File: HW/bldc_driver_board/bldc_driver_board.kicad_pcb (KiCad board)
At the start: 2 copper layers, 80 x 119.4 mm, 55 parts, among them IC1 DRV8305NPHPR, J1 PWR, J2 N_CN7, J3 N_CN10, J5 Motor, J6 RJ45, J7 RJ45, Q1 STD140N6F7, Q2 STD140N6F7, Q3 STD140N6F7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

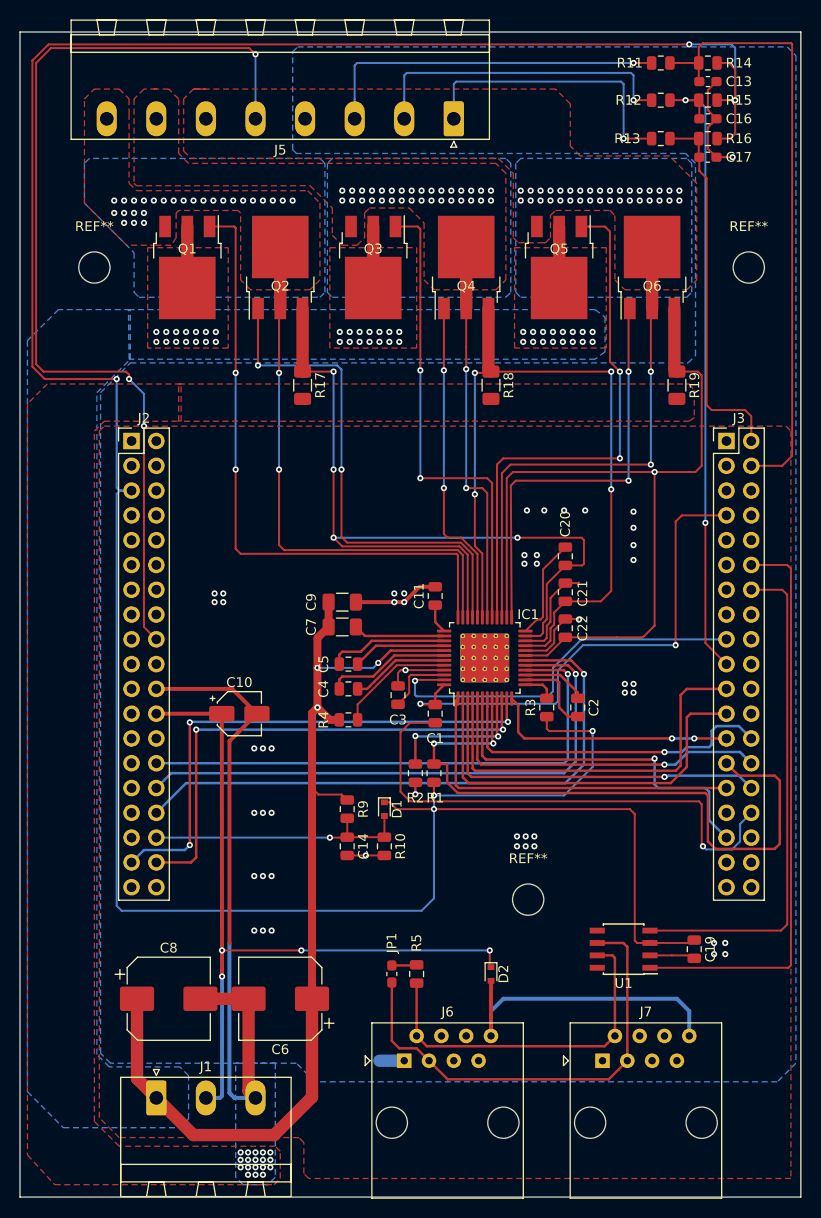
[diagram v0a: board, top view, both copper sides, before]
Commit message: -- Added panels for drill holes
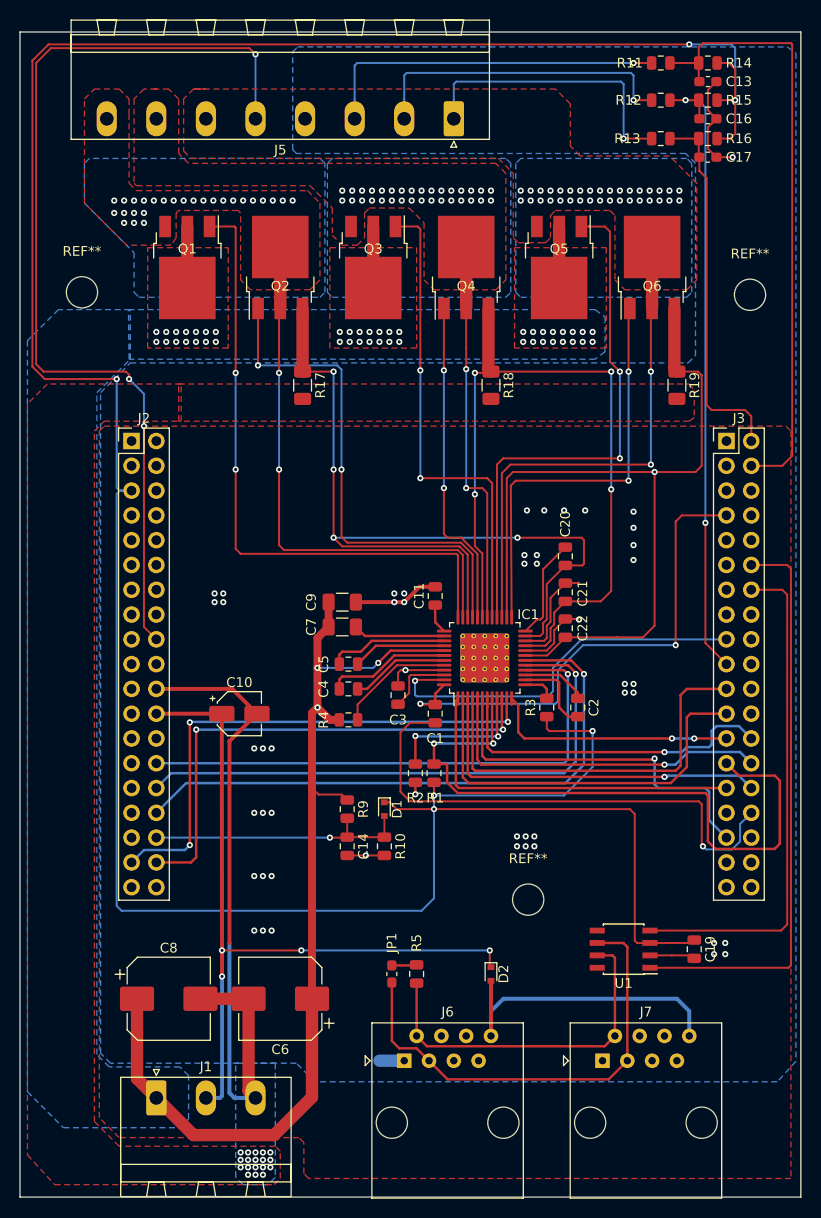
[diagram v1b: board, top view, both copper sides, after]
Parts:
- moved REF** 2.84 mm to (38.1, 73.7)
- moved REF** 2.80 mm to (106.6, 73.9)
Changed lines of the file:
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@@
   )
   (module MountingHole:MountingHole_3.2mm_M3 (layer F.Cu)
-    (at 39.37 71.12)
+    (at 38.1 73.66)
     (descr "Mounting Hole 3.2mm, no annular, M3")
     (tags "mounting hole 3.2mm no annular m3")
@@
   )
   (module MountingHole:MountingHole_3.2mm_M3 (layer F.Cu)
-    (at 106.426 71.12)
+    (at 106.553 73.914)
     (descr "Mounting Hole 3.2mm, no annular, M3")
     (tags "mounting hole 3.2mm no annular m3")
@@
         (xy 43.053 80.899) (xy 100.203 80.899) (xy 100.965 80.137) (xy 100.965 60.452) (xy 99.949 59.436)
         (xy 60.071 59.436) (xy 59.69 59.055) (xy 59.69 49.022) (xy 60.198 48.514) (xy 110.363 48.514)
-        (xy 111.252 49.403) (xy 111.252 152.654) (xy 109.347 154.559)
+        (xy 111.252 49.149) (xy 111.252 152.4635) (xy 109.347 154.559)
       )
     )
@@
       )
     )
+  )
+  (zone (net 0) (net_name "") (layers F&B.Cu) (hatch full 0.508)
+    (connect_pads (clearance 0.813))
+    (min_thickness 0.254)
+    (keepout (tracks not_allowed) (vias not_allowed) (copperpour not_allowed))
+    (fill (arc_segments 16) (thermal_gap 0.508) (thermal_bridge_width 0.508))
+    (polygon
+      (pts
+        (xy 80.01 139.192) (xy 80.01 132.588) (xy 80.264 132.334) (xy 80.518 132.08) (xy 87.249 132.08)
+        (xy 87.503 132.334) (xy 87.63 132.461) (xy 87.63 139.319) (xy 87.503 139.446) (xy 87.249 139.7)
+        (xy 80.518 139.7) (xy 80.264 139.446)
+      )
+    )
+  )
+  (zone (net 0) (net_name "") (layers F&B.Cu) (hatch edge 0.508)
+    (connect_pads (clearance 0.813))
+    (min_thickness 0.254)
+    (keepout (tracks not_allowed) (vias not_allowed) (copperpour not_allowed))
+    (fill (arc_segments 16) (thermal_gap 0.508) (thermal_bridge_width 0.508))
+    (polygon
+      (pts
+        (xy 109.728 70.104) (xy 102.743 70.104) (xy 102.743 70.739) (xy 102.743 77.597) (xy 109.728 77.597)
+        (xy 110.109 77.216) (xy 110.236 77.089) (xy 110.236 70.612) (xy 109.982 70.358)
+      )
+    )
+  )
+  (zone (net 0) (net_name "") (layers F&B.Cu) (hatch edge 0.508)
+    (connect_pads (clearance 0.813))
+    (min_thickness 0.254)
+    (keepout (tracks not_allowed) (vias not_allowed) (copperpour not_allowed))
+    (fill (arc_segments 16) (thermal_gap 0.508) (thermal_bridge_width 0.508))
+    (polygon
+      (pts
+        (xy 34.29 76.962) (xy 34.29 69.85) (xy 42.418 69.85) (xy 42.418 75.438) (xy 41.91 75.946)
+        (xy 41.91 76.962) (xy 41.402 77.47) (xy 34.798 77.47)
+      )
+    )

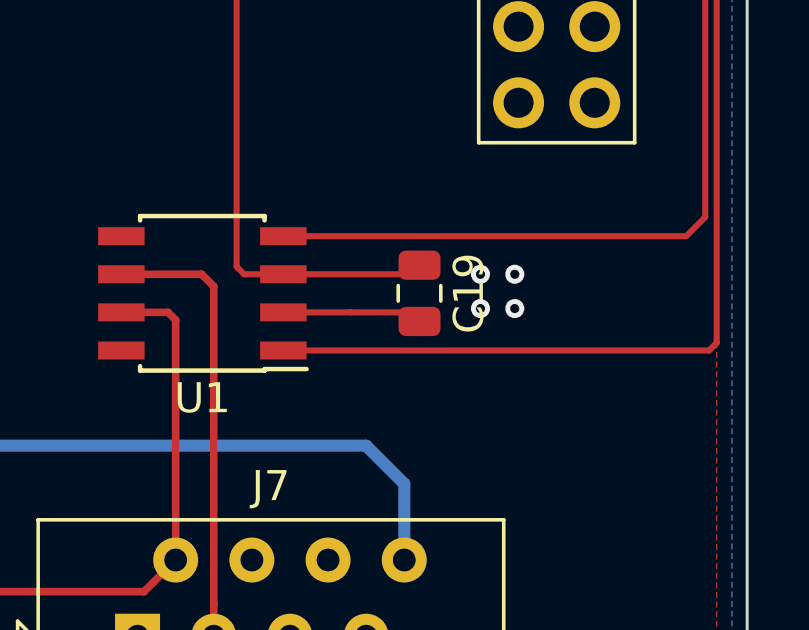
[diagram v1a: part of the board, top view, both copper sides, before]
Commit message: -- Fixed unwired CAN chip
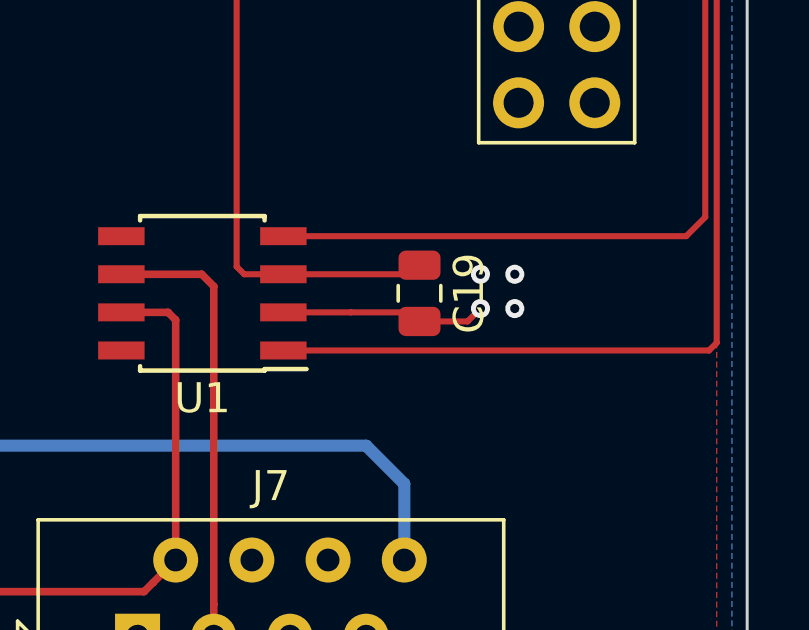
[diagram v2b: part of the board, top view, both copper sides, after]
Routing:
- net GND: track 144.6 -> 146.8 mm
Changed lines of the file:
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@@
     (thickness 1.6)
     (drawings 6)
-    (tracks 859)
+    (tracks 861)
     (zones 0)
     (modules 55)
@@
   (via (at 83.566 130.429) (size 0.635) (drill 0.3048) (layers F.Cu B.Cu) (net 4))
   (via (at 82.677 130.429) (size 0.635) (drill 0.3048) (layers F.Cu B.Cu) (net 4))
+  (segment (start 102.4405 141.9075) (end 102.87 141.478) (width 0.2032) (layer F.Cu) (net 4))
+  (segment (start 100.838 141.9075) (end 102.4405 141.9075) (width 0.2032) (layer F.Cu) (net 4))
   (segment (start 75.2125 112.875) (end 71.783 112.875) (width 0.2032) (layer F.Cu) (net 5))
   (segment (start 71.783 112.875) (end 71.628 113.03) (width 0.2032) (layer F.Cu) (net 5))

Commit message: -- Added Gerber Files for JBLPCB Production
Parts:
- REF** (x3): value MountingHole_3.2mm_M3 -> (none)
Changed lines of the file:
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@@
   (general
     (thickness 1.6)
-    (drawings 6)
+    (drawings 4)
     (tracks 861)
     (zones 0)
@@
     (0 F.Cu signal)
     (31 B.Cu signal)
-    (32 B.Adhes user)
-    (33 F.Adhes user)
+    (32 B.Adhes user hide)
+    (33 F.Adhes user hide)
     (34 B.Paste user)
     (35 F.Paste user)
@@
     (38 B.Mask user)
     (39 F.Mask user)
-    (40 Dwgs.User user)
-    (41 Cmts.User user)
-    (42 Eco1.User user)
-    (43 Eco2.User user)
+    (40 Dwgs.User user hide)
+    (41 Cmts.User user hide)
+    (42 Eco1.User user hide)
+    (43 Eco2.User user hide)
     (44 Edge.Cuts user)
-    (45 Margin user)
+    (45 Margin user hide)
     (46 B.CrtYd user)
     (47 F.CrtYd user)
-    (48 B.Fab user)
+    (48 B.Fab user hide)
     (49 F.Fab user hide)
   )
@@
     (aux_axis_origin 0 0)
     (grid_origin 31.75 166.37)
-    (visible_elements 7FFFFFFF)
+    (visible_elements 7EFFFFFF)
     (pcbplotparams
-      (layerselection 0x010fc_ffffffff)
+      (layerselection 0x0d0fc_ffffffff)
       (usegerberextensions false)
-      (usegerberattributes false)
-      (usegerberadvancedattributes false)
+      (usegerberattributes true)
+      (usegerberadvancedattributes true)
       (creategerberjobfile false)
-      (excludeedgelayer true)
-      (linewidth 0.100000)
+      (excludeedgelayer false)
+      (linewidth 0.150000)
       (plotframeref false)
       (viasonmask false)
@@
       (plotvalue true)
       (plotinvisibletext false)
-      (padsonsilk false)
+      (padsonsilk true)
       (subtractmaskfromsilk false)
       (outputformat 1)
       (mirror false)
-      (drillshape 1)
+      (drillshape 0)
       (scaleselection 1)
-      (outputdirectory ""))
+      (outputdirectory "gerber/"))
   )
   (net 0 "")
@@
       (effects (font (size 1 1) (thickness 0.15)))
     )
-    (fp_text value MountingHole_3.2mm_M3 (at 0 4.2) (layer F.Fab)
+    (fp_text value "" (at 0 4.2) (layer F.Fab)
       (effects (font (size 1 1) (thickness 0.15)))
     )
@@
       (effects (font (size 1 1) (thickness 0.15)))
     )
-    (fp_text value MountingHole_3.2mm_M3 (at 0 4.2) (layer F.Fab)
+    (fp_text value "" (at 0 4.2) (layer F.Fab)
       (effects (font (size 1 1) (thickness 0.15)))
     )
@@
       (effects (font (size 1 1) (thickness 0.15)))
     )
-    (fp_text value MountingHole_3.2mm_M3 (at 0 4.2) (layer F.Fab)
+    (fp_text value "" (at 0 4.2) (layer F.Fab)
       (effects (font (size 1 1) (thickness 0.15)))
     )
@@
     (pad 1 np_thru_hole circle (at 0 0) (size 3.2 3.2) (drill 3.2) (layers *.Cu *.Mask))
   )
-  (dimension 80.01 (width 0.3) (layer F.SilkS)
-    (gr_text "80,010 mm" (at 71.755 177.614) (layer F.SilkS)
-      (effects (font (size 1.5 1.5) (thickness 0.3)))
-    )
-    (feature1 (pts (xy 111.76 166.37) (xy 111.76 176.100421)))
-    (feature2 (pts (xy 31.75 166.37) (xy 31.75 176.100421)))
-    (crossbar (pts (xy 31.75 175.514) (xy 111.76 175.514)))
-    (arrow1a (pts (xy 111.76 175.514) (xy 110.633496 176.100421)))
-    (arrow1b (pts (xy 111.76 175.514) (xy 110.633496 174.927579)))
-    (arrow2a (pts (xy 31.75 175.514) (xy 32.876504 176.100421)))
-    (arrow2b (pts (xy 31.75 175.514) (xy 32.876504 174.927579)))
-  )
-  (dimension 119.38 (width 0.3) (layer F.SilkS)
-    (gr_text "119,380 mm" (at 15.68 106.68 270) (layer F.SilkS)
-      (effects (font (size 1.5 1.5) (thickness 0.3)))
-    )
-    (feature1 (pts (xy 31.75 166.37) (xy 17.193579 166.37)))
-    (feature2 (pts (xy 31.75 46.99) (xy 17.193579 46.99)))
-    (crossbar (pts (xy 17.78 46.99) (xy 17.78 166.37)))
-    (arrow1a (pts (xy 17.78 166.37) (xy 17.193579 165.243496)))
-    (arrow1b (pts (xy 17.78 166.37) (xy 18.366421 165.243496)))
-    (arrow2a (pts (xy 17.78 46.99) (xy 17.193579 48.116504)))
-    (arrow2b (pts (xy 17.78 46.99) (xy 18.366421 48.116504)))
-  )
   (gr_line (start 31.75 166.37) (end 31.75 46.99) (layer Edge.Cuts) (width 0.1))

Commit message: -- Fixed missing nSCS pin error
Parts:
- removed R2: 10k, Resistor_SMD:R_0805_2012Metric
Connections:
- IC1 pad 9: Net-(IC1-Pad9) -> /~SCS
- J2 pad 37: Net-(J2-Pad37) -> /~SCS
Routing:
- net /~SCS: track 0.00 -> 57.5 mm, vias 0 -> 1
- net Net-(IC1-Pad9): track 15.3 -> 0.00 mm, vias 2 -> 0
- net GND: track 146.8 -> 145.6 mm, vias 69 -> 68
